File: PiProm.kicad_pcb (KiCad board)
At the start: 2 copper layers, 50.8 x 56.9 mm, 38 parts, among them J1 Raspberry_Pi_2_3, J2 Conn_01x02_Male, Q1 BSS84, SW1 SW_Push, SW2 SW_Push, U1 4040, U2 4040, U3 GTL2000, U4 27C160, U5 LM317L_SO8, U6 AP3012, U7 PT4101

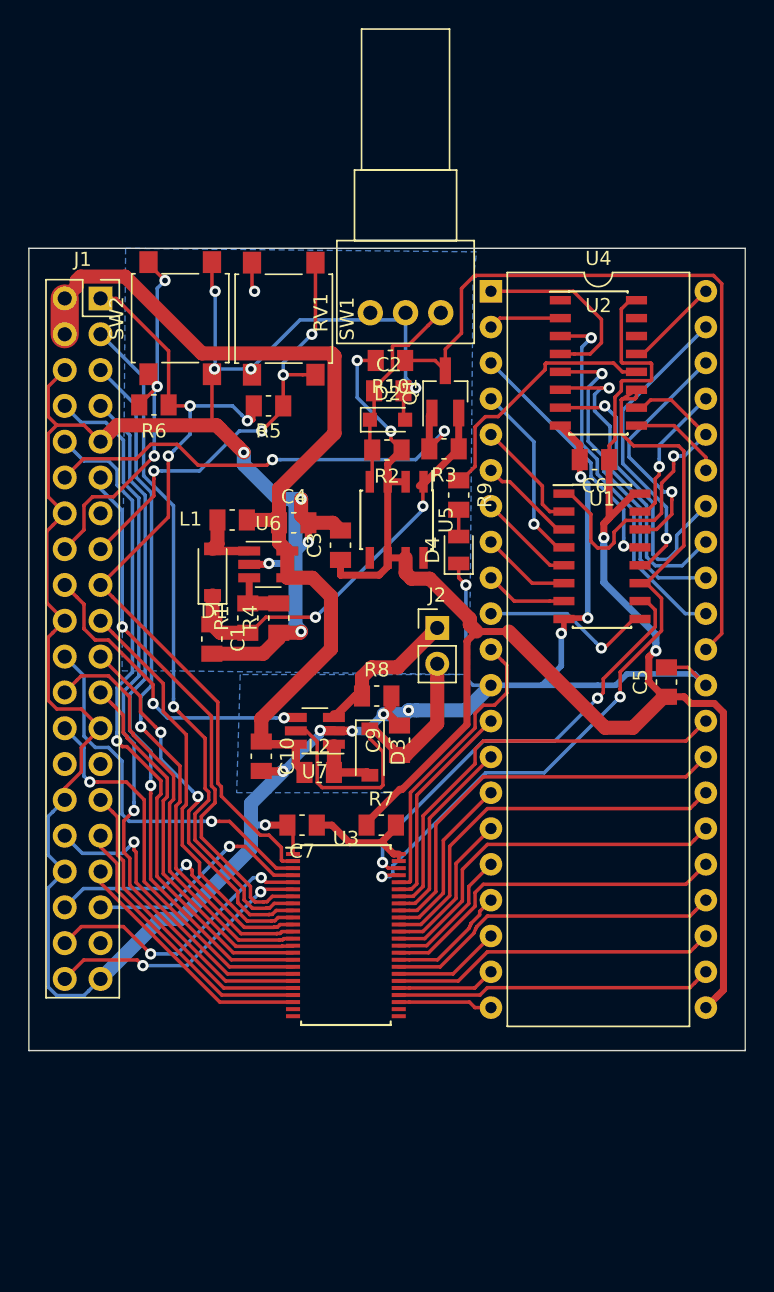
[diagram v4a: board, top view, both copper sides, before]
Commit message: - Moved LED driver to second stage board - Fixed direction of Pi GPIO connector
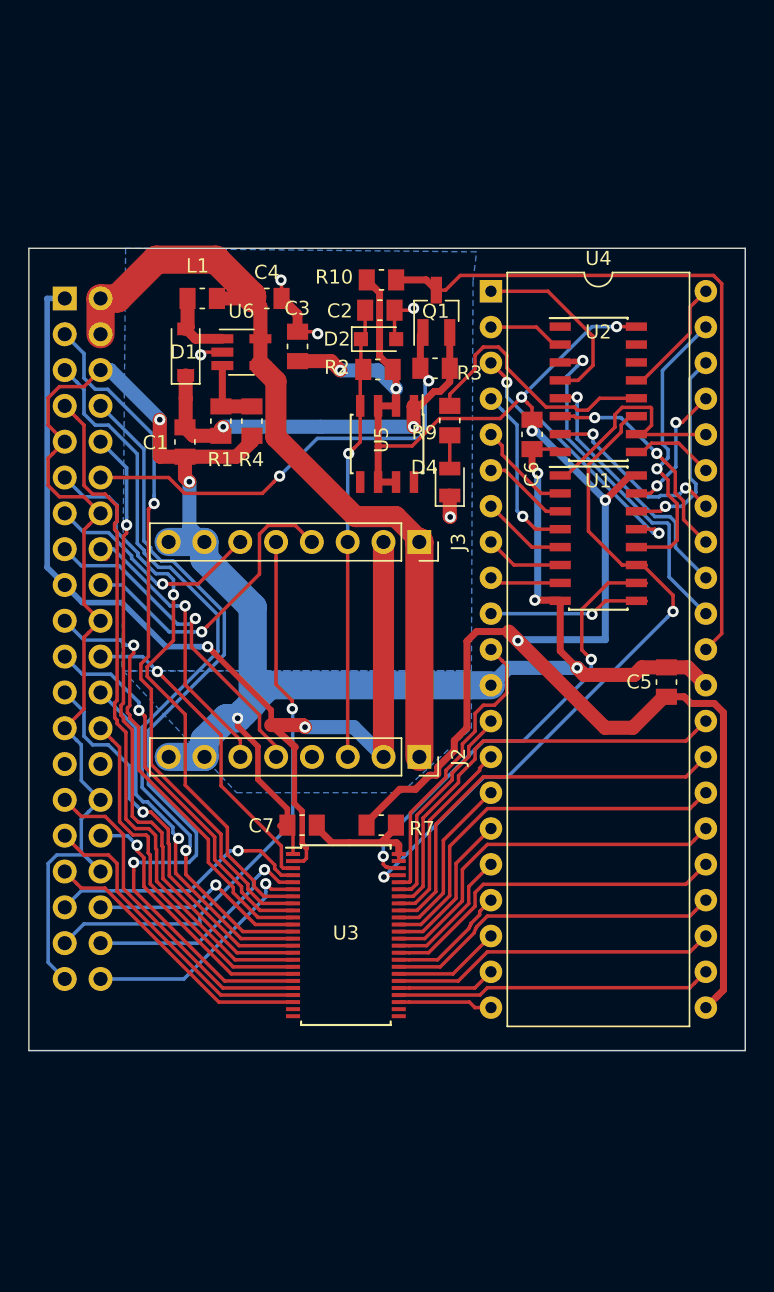
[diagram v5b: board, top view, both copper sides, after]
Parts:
- removed C10, C9: 10u, Capacitor_SMD:C_0805_2012Metric_Pad1.15x1.50mm_HandSolder
- removed D3: SB120, Diode_SMD:D_SOD-123
- removed L2: 2u2, Inductor_SMD:L_0805_2012Metric_Pad1.15x1.50mm_HandSolder
- removed R5, R6: R, Resistor_SMD:R_0805_2012Metric_Pad1.15x1.50mm_HandSolder
- removed R8: 5.28, Resistor_SMD:R_0805_2012Metric_Pad1.15x1.50mm_HandSolder
- removed RV1: 10k, Potentiometer_THT:Potentiometer_Alps_RK097_Single_Horizontal
- removed SW1, SW2: SW_Push, Button_Switch_SMD:SW_SPST_B3S-1000
- removed U7: PT4101, Package_TO_SOT_SMD:SOT-23-6_Handsoldering
- added J3: Conn_01x08_Female, Connector_PinSocket_2.54mm:PinSocket_1x08_P2.54mm_Vertical, F.Cu at (40.4, 35.1)
- J1: moved to B.Cu
- J2: value Conn_01x02_Male -> Conn_01x08_Female; footprint Connector_PinHeader_2.54mm:PinHeader_1x02_P2.54mm_Vertical -> Connector_PinSocket_2.54mm:PinSocket_1x08_P2.54mm_Vertical
- moved C4 16.0 mm to (29.6, 17.8)
- moved L1 15.9 mm to (25.0, 17.8)
- moved D1 15.7 mm to (23.8, 21.6)
- moved U6 15.2 mm to (27.8, 21.6)
- moved C3 14.4 mm to (31.8, 21.2)
- moved C1 14.1 mm to (23.8, 28.0)
- moved R1 14.1 mm to (26.3, 26.5)
- moved R4 14.1 mm to (28.5, 26.5)
- moved J2 9.23 mm to (40.4, 50.3), turned to 270 degrees
- moved D2 5.75 mm to (37.5, 20.7)
- moved R3 5.75 mm to (41.5, 22.7)
- moved C2 5.75 mm to (37.6, 18.6)
- moved Q1 5.75 mm to (41.6, 18.7)
- moved R10 5.75 mm to (37.7, 16.5)
- moved R2 5.75 mm to (37.5, 22.8)
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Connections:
- C2 pad 1: Net-(C2-Pad1) -> /VCC_ADJ
- D2 pad 1: Net-(C2-Pad1) -> /VCC_ADJ
- J1 pad 13: Net-(J1-Pad13) -> /BUTTON4
- J1 pad 37: Net-(J1-Pad37) -> /BUTTON3
- J2 pad 1: Net-(J2-Pad1) -> +5V
- J2 pad 2: Net-(C9-Pad1) -> +3V3
- R2 pad 2: Net-(C2-Pad1) -> /VCC_ADJ
- U5 pad 4: Net-(C2-Pad1) -> /VCC_ADJ
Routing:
- net GND: track 242.7 -> 183.5 mm, vias 20 -> 11
- net /BUTTON3: track 0.00 -> 40.4 mm, vias 0 -> 1
- net /VCC_ADJ: track 0.00 -> 32.5 mm, vias 0 -> 1
- net Net-(C9-Pad1): track 24.7 -> 0.00 mm
- net +3V3: track 59.1 -> 77.2 mm, vias 3 -> 2
- net /BUTTON4: track 0.00 -> 15.9 mm, vias 0 -> 1
- net Net-(C2-Pad1): track 14.8 -> 0.00 mm
- net Net-(J2-Pad1): track 11.0 -> 0.00 mm
- net +5V: track 65.6 -> 57.3 mm
- net /A11: track 24.6 -> 16.5 mm, vias 1 -> 0
- net /A13: track 21.2 -> 13.3 mm, vias 1 -> 2
- net /BUTTON1: track 31.7 -> 24.0 mm, vias 4 -> 1
- net /GPIO14: track 52.8 -> 60.2 mm
- net /A14: track 22.9 -> 15.7 mm, vias 1 -> 2
- net /BUTTON2: track 27.6 -> 21.3 mm, vias 3 -> 1
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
